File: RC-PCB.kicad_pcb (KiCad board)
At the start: 2 copper layers, 30 x 65 mm, 32 parts

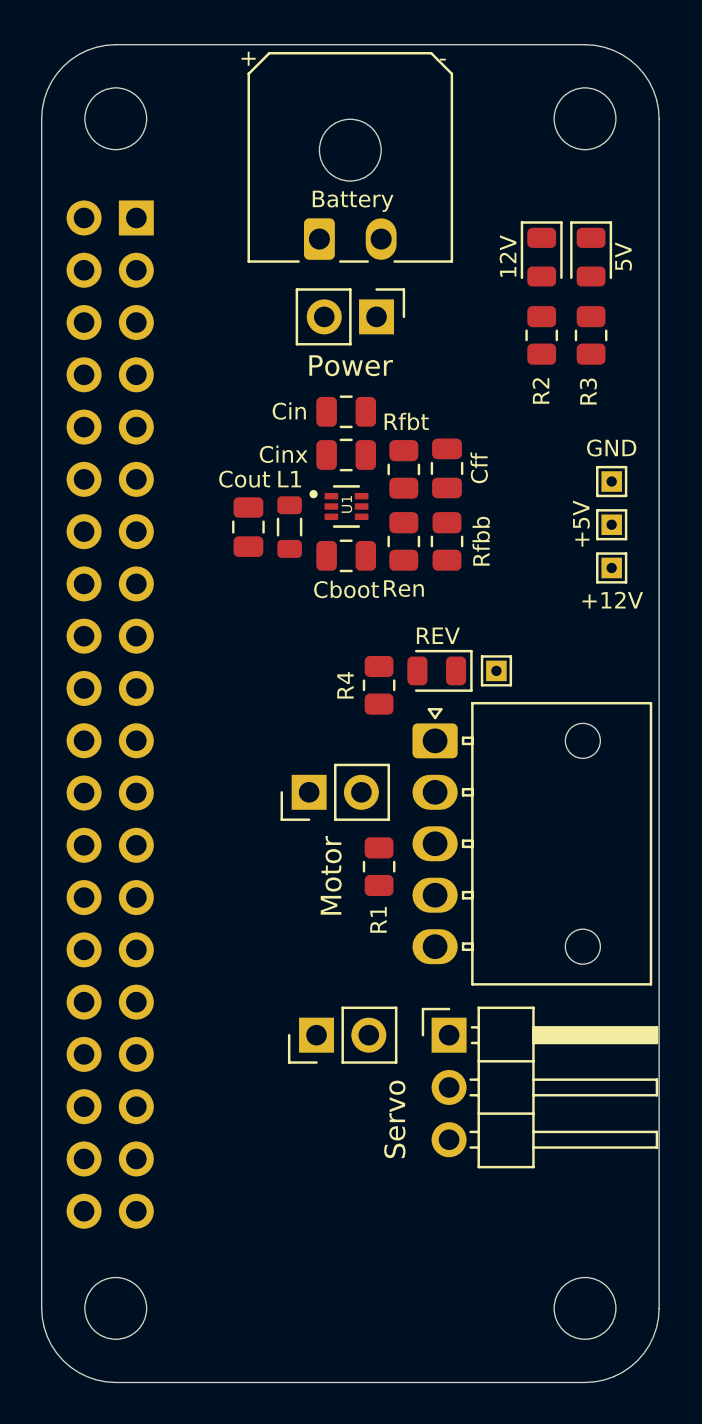
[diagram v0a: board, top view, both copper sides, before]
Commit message: fixed fins, moved stuff around
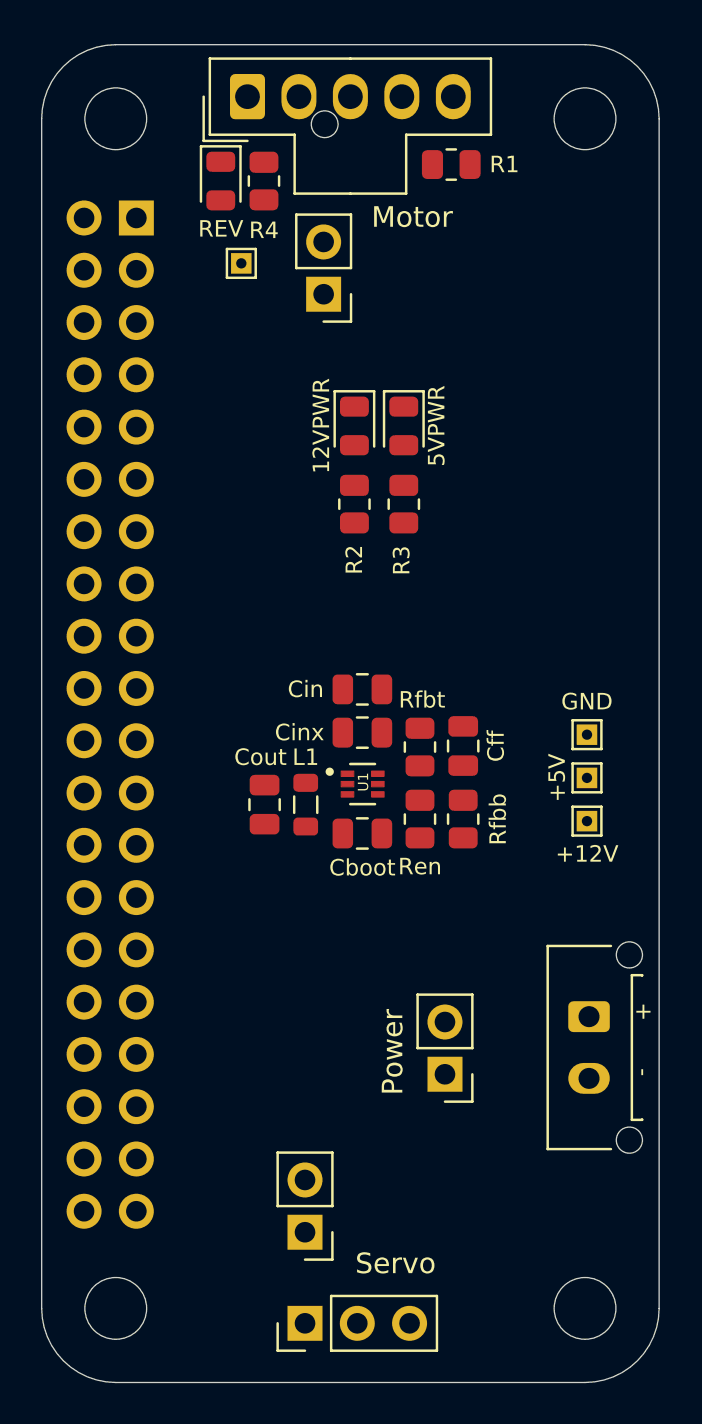
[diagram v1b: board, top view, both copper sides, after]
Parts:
- Battery1: renamed from Battery; footprint Connector_Molex:Molex_Micro-Fit_3.0_43650-0200_1x02_P3.00mm_Horizontal -> Connector_Molex:Molex_Micro-Fit_3.0_43650-0215_1x02_P3.00mm_Vertical
- Motor1: renamed from Motor; footprint Connector_Molex:Molex_Nano-Fit_105313-xx05_1x05_P2.50mm_Horizontal -> Connector_Molex:Molex_Nano-Fit_105309-xx05_1x05_P2.50mm_Vertical
- Servo1: footprint Connector_PinHeader_2.54mm:PinHeader_1x03_P2.54mm_Horizontal -> Connector_PinHeader_2.54mm:PinHeader_1x03_P2.54mm_Vertical
- moved Battery1 40.0 mm to (160.9, 120.5), turned to -90 degrees
- moved Power 36.9 mm to (153.9, 123.3), turned to 180 degrees
- moved R1 34.3 mm to (154.2, 79.1), turned to 0 degrees
- moved Motor1 32.6 mm to (144.3, 75.8), turned to 90 degrees
- moved REV 26.0 mm to (143.0, 79.9), turned to -90 degrees
- moved R4 25.1 mm to (145.1, 79.9), turned to -90 degrees
- moved Motor 24.2 mm to (148.0, 85.4), turned to 180 degrees
- moved Rev2 23.4 mm to (144.0, 83.9), turned to 90 degrees
- moved Servo1 15.7 mm to (147.1, 135.4), turned to 90 degrees
- moved Ren 13.5 mm to (152.7, 110.9)
- moved Rfbb 13.5 mm to (154.8, 110.9)
- moved Rfbt 13.5 mm to (152.7, 107.4)
- moved Cboot 13.5 mm to (149.9, 111.6)
- moved Cff 13.5 mm to (154.8, 107.3)
- moved Cin 13.5 mm to (149.9, 104.6)
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- renumbered 12V to 12VPWR, 5V to 5VPWR, GPIO to GPIO1, Rev to Rev2
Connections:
- GPIO1 pad 1: unconnected-(GPIO1-Pin_1-Pad1) -> GND
- GPIO1 pad 12: unconnected-(GPIO1-Pin_12-Pad12) -> GND
- GPIO1 pad 14: GND -> unconnected-(GPIO1-Pin_14-Pad14)
- GPIO1 pad 15: /Rev -> GND
- GPIO1 pad 16: /Servo_PWM -> unconnected-(GPIO1-Pin_16-Pad16)
- GPIO1 pad 18: /Motor_PWM -> unconnected-(GPIO1-Pin_18-Pad18)
- GPIO1 pad 2: +5V -> unconnected-(GPIO1-Pin_2-Pad2)
- GPIO1 pad 20: GND -> unconnected-(GPIO1-Pin_20-Pad20)
- GPIO1 pad 22: unconnected-(GPIO1-Pin_22-Pad22) -> GND
- GPIO1 pad 24: unconnected-(GPIO1-Pin_24-Pad24) -> /Motor_PWM
- GPIO1 pad 25: GND -> /Rev
- GPIO1 pad 26: unconnected-(GPIO1-Pin_26-Pad26) -> /Servo_PWM
- GPIO1 pad 28: unconnected-(GPIO1-Pin_28-Pad28) -> GND
- GPIO1 pad 30: GND -> unconnected-(GPIO1-Pin_30-Pad30)
- GPIO1 pad 31: unconnected-(GPIO1-Pin_31-Pad31) -> GND
- GPIO1 pad 34: GND -> unconnected-(GPIO1-Pin_34-Pad34)
- GPIO1 pad 36: unconnected-(GPIO1-Pin_36-Pad36) -> GND
- GPIO1 pad 38: unconnected-(GPIO1-Pin_38-Pad38) -> +5V
- GPIO1 pad 39: GND -> unconnected-(GPIO1-Pin_39-Pad39)
- GPIO1 pad 4: +5V -> unconnected-(GPIO1-Pin_4-Pad4)
- GPIO1 pad 40: unconnected-(GPIO1-Pin_40-Pad40) -> +5V
- GPIO1 pad 6: GND -> unconnected-(GPIO1-Pin_6-Pad6)
- GPIO1 pad 8: unconnected-(GPIO1-Pin_8-Pad8) -> GND
- GPIO1 pad 9: GND -> unconnected-(GPIO1-Pin_9-Pad9)
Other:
- board text added: "Camera side"

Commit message: finished routing
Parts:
- moved Servo 3.41 mm to (147.1, 127.6), turned to 0 degrees
- moved Motor 2.57 mm to (150.6, 85.4), turned to -90 degrees
- moved Cinx 2.34 mm to (148.8, 104.6)
- moved Cout 2.34 mm to (144.1, 108.1)
- moved L1 2.34 mm to (146.1, 108.1)
- moved Ren 2.34 mm to (151.7, 108.8)
- moved Rfbb 2.34 mm to (153.8, 108.8)
- moved Rfbt 2.34 mm to (151.7, 105.3)
- moved U1 2.34 mm to (148.9, 107.1)
- moved Cboot 2.34 mm to (148.8, 109.5)
- moved Cff 2.34 mm to (153.8, 105.2)
- moved Cin 2.34 mm to (148.8, 102.5)
- moved +5V 1.84 mm to (160.4, 107.1)
- moved +12V 1.84 mm to (160.4, 109.2)
- moved GND 1.84 mm to (160.4, 105.0)
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- renumbered 12VPWR to 12V, 5VPWR to 5V, GPIO1 to GPIO, R1 to R
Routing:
- net +12V: track 0.00 -> 67.6 mm, vias 0 -> 3
- net GND: track 0.00 -> 56.7 mm, vias 0 -> 7
- net /Rev: track 0.00 -> 48.4 mm
- net /Motor_PWM: track 0.00 -> 36.7 mm
- net /Servo_PWM: track 0.00 -> 20.6 mm, vias 0 -> 2
- net Net-(Motor1-Pin_2): track 0.00 -> 10.1 mm
- net Net-(Battery1-Pin_1): track 0.00 -> 7.61 mm
- net Net-(Motor1-Pin_3): track 0.00 -> 6.24 mm
- net Net-(U1-FB): track 0.00 -> 6.00 mm
- net Net-(Servo1-Pin_1): track 0.00 -> 5.30 mm
- net Net-(U1-SW): track 0.00 -> 5.26 mm
- net Net-(U1-EN): track 0.00 -> 2.38 mm
- net Net-(REV1-A): track 0.00 -> 2.11 mm
- net Net-(U1-BST): track 0.00 -> 1.98 mm
- net Net-(5VPWR1-A): track 0.00 -> 1.95 mm
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- added copper zone on F.Cu, net +5V
- added copper zone on B.Cu, net GND
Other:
- board text added: "5V"

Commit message: ready to order
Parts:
- 12V, 5V: footprint LED_SMD:LED_0805_2012Metric -> LED_SMD:LED_0805_2012Metric_Pad1.15x1.40mm_HandSolder
- Cboot, Cff, Cin, Cinx, Cout: footprint Capacitor_SMD:C_0805_2012Metric -> Capacitor_SMD:C_0805_2012Metric_Pad1.18x1.45mm_HandSolder
- L1: footprint Inductor_SMD:L_0805_2012Metric -> Inductor_SMD:L_1008_2520Metric_Pad1.43x2.20mm_HandSolder
- R0: renamed from R; footprint Resistor_SMD:R_0805_2012Metric -> Resistor_SMD:R_0805_2012Metric_Pad1.20x1.40mm_HandSolder
- R2, R3, Ren, Rfbb, Rfbt: footprint Resistor_SMD:R_0805_2012Metric -> Resistor_SMD:R_0805_2012Metric_Pad1.20x1.40mm_HandSolder
- R4: value 650 -> 620; footprint Resistor_SMD:R_0805_2012Metric -> Resistor_SMD:R_0805_2012Metric_Pad1.20x1.40mm_HandSolder
- REV1: renamed from REV; value LED -> REV; footprint LED_SMD:LED_0805_2012Metric -> LED_SMD:LED_0805_2012Metric_Pad1.15x1.40mm_HandSolder
- moved Cout 2.30 mm to (141.8, 108.1)
- moved L1 1.22 mm to (144.9, 108.3)
- moved Cff 0.43 mm to (154.0, 104.9)
- moved Rfbt 0.39 mm to (151.9, 105.0)
- moved Ren 0.32 mm to (151.9, 109.0)
- moved Rfbb 0.32 mm to (154.0, 109.0)
- moved R0 0.31 mm to (154.5, 79.2)
- moved R4 0.20 mm to (145.1, 80.1)
- moved REV1 0.20 mm to (143.0, 80.1)
- moved R2 0.09 mm to (148.1, 96.3)
- moved R3 0.09 mm to (150.5, 96.3)
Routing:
- net Net-(U1-SW): track 5.26 -> 7.14 mm
- net +12V: track 67.6 -> 68.9 mm, vias 3 -> 2
- net /Rev: track 48.4 -> 49.2 mm
- net Net-(U1-FB): track 6.00 -> 6.74 mm
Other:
- board text added: "R"
- board text added: "~"

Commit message: ready to order pt 2
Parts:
- added C1: .1uF, Capacitor_SMD:C_0805_2012Metric_Pad1.18x1.45mm_HandSolder, F.Cu at (154.5, 79.2)
- added C2: 10uF, Capacitor_SMD:C_0805_2012Metric_Pad1.18x1.45mm_HandSolder, F.Cu at (154.5, 81.4)
- added C3: 10uF, Capacitor_SMD:C_0805_2012Metric_Pad1.18x1.45mm_HandSolder, B.Cu at (154.5, 81.4)
- added C4: .1uF, Capacitor_SMD:C_0805_2012Metric_Pad1.18x1.45mm_HandSolder, F.Cu at (152.0, 132.5)
- added C5: 10uF, Capacitor_SMD:C_0805_2012Metric_Pad1.18x1.45mm_HandSolder, F.Cu at (152.0, 130.4)
- added C6: 10uF, Capacitor_SMD:C_0805_2012Metric_Pad1.18x1.45mm_HandSolder, B.Cu at (152.0, 130.4)
- moved R1 5.16 mm to (150.3, 82.2)
- renumbered R0 to R1
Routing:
- net +12V: track 68.9 -> 67.3 mm, vias 2 -> 3
- net GND: vias 7 -> 11
- net +5V: vias 0 -> 1
